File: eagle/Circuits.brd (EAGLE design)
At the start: 160 x 100 mm, 45 parts, among them IC1 74AC14N, IC2 mcp603, IC5 PCF8574P, X1 JP1

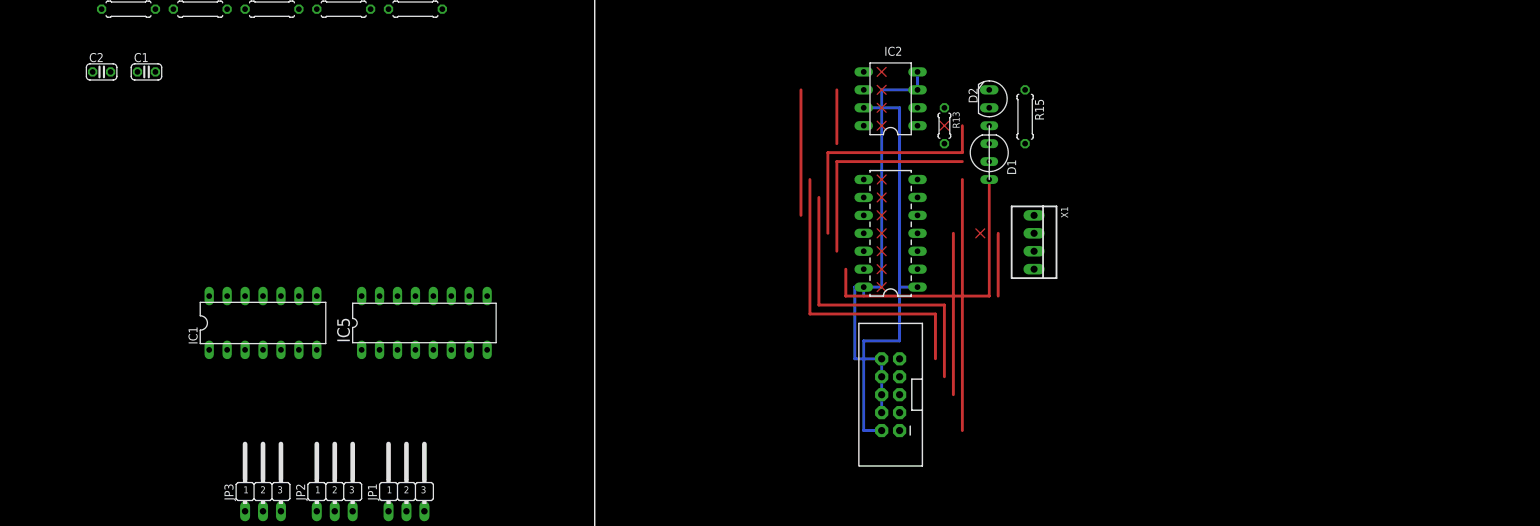
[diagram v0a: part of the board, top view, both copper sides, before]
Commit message: Added PIC colour sensor as DA Backup
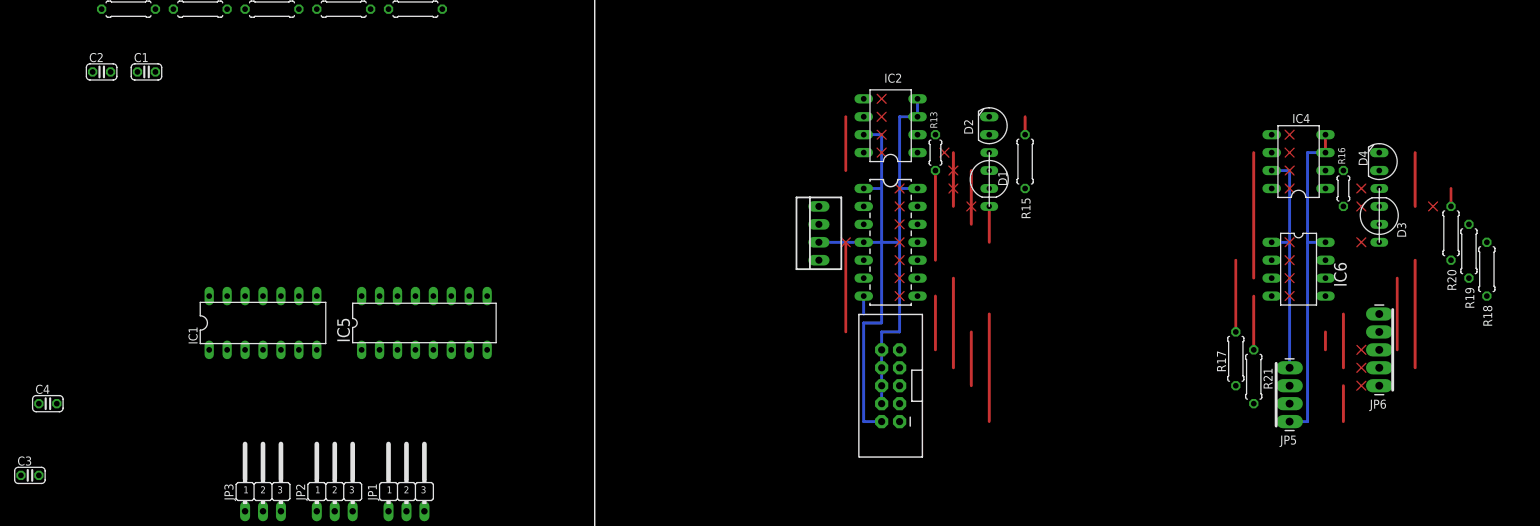
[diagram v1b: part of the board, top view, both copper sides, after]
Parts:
- added C3: 16pF, resistor:C025-024X044
- added C4: 22pF, resistor:C025-024X044
- added D3: LED-RGB-CC-THRUCLEAR, SparkFun-LED:LED-RGB-THRU
- added D4: SFH213, opto-trans-siemens:SFH205
- added IC4: mcp603, analog-devices:DIL08
- added IC6: PIC12F675P, microchip:DIL8
- added JP5: (no value), SparkFun-Connectors:1X04_LONGPADS
- added JP6: (no value), SparkFun-Connectors:1X05_LONGPADS
- added R16: 1M, resistor:0204/5
- added R17, R21: 10k, resistor:0207/7
- added R18, R19, R20: 220, resistor:0207/7
- added U$16, U$17, U$18, U$19, U$2, U$20, U$21, U$22, U$23, U$24, U$25, U$26, U$27, U$28, U$29, U$30, U$31, U$32: (no value), Joe Roberts:BREAK
- moved X1 30.5 mm to (31.8, 41.9), turned to 90 degrees
- moved U$15 7.41 mm to (50.8, 48.3)
- moved R15 6.35 mm to (61.0, 52.1)
- moved D1 5.08 mm to (55.9, 48.9), turned to 270 degrees
- moved R13 4.02 mm to (48.3, 53.3)
- moved D2 3.81 mm to (55.9, 57.1)
- moved IC2 3.81 mm to (41.9, 57.1)
- moved U$1 3.81 mm to (41.9, 39.4), turned to 270 degrees
- moved U$10 3.81 mm to (40.6, 53.3)
- moved U$11 3.81 mm to (40.6, 55.9)
- moved U$12 3.81 mm to (40.6, 58.4)
- moved U$13 3.81 mm to (40.6, 61.0)
- moved U$14 3.81 mm to (49.5, 53.3)
- moved U$7 2.84 mm to (43.2, 43.2)
- moved U$8 2.84 mm to (43.2, 45.7)
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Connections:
- removed net N$21: U$1.5, X1.1
- new net N$22: D3.4, R18.1
- new net N$23: D3.3, R19.1
- new net N$24: IC6.2, R17.2
- new net N$25: C3.1, D4.A, IC4.2, R16.1
- new net N$28: D3.1, R20.1
- new net N$29: IC6.5, R18.2
- new net PROG-CLK: IC6.6, JP6.3, R19.2
- new net PROG-IO: IC6.7, JP6.4, R20.2
- new net VPP: IC6.4, JP6.2, R21.1
- net +5V: now also C4.2, IC4.7, IC6.1, JP5.1, JP6.1
- net COLOUR-1: now also JP5.3, R21.2, U$1.5, X1.1
- net COLOUR-2: now also JP5.2, R17.1
- net GND: now also C4.1, D3.2, D4.K, IC4.3, IC4.4, IC6.8, JP5.4, JP6.5
- net PHOTO_OUT: now also C3.2, IC4.6, IC6.3, R16.2
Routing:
- net GND: track 71.1 -> 125.7 mm
- net MISO: track 43.2 -> 7.62 mm
- net N$3: track 40.6 -> 7.62 mm
- net SCK: track 43.2 -> 12.7 mm
- net +5V: track 61.0 -> 91.4 mm
- net N$18: track 34.3 -> 5.08 mm
- net N$7: track 30.5 -> 7.62 mm
- net MOSI: track 35.6 -> 17.8 mm
- net PROG-IO: track 0.00 -> 15.2 mm
- net PHOTO_OUT: track 25.4 -> 38.1 mm
- net VPP: track 0.00 -> 10.2 mm
- net PROG-CLK: track 0.00 -> 10.2 mm
- net N$24: track 0.00 -> 10.2 mm
- net N$28: track 0.00 -> 2.54 mm
- net RESET: track 22.9 -> 20.3 mm
